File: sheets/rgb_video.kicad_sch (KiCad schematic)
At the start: 46 parts, among them CN3 DIN-8, U32 CXA1145P

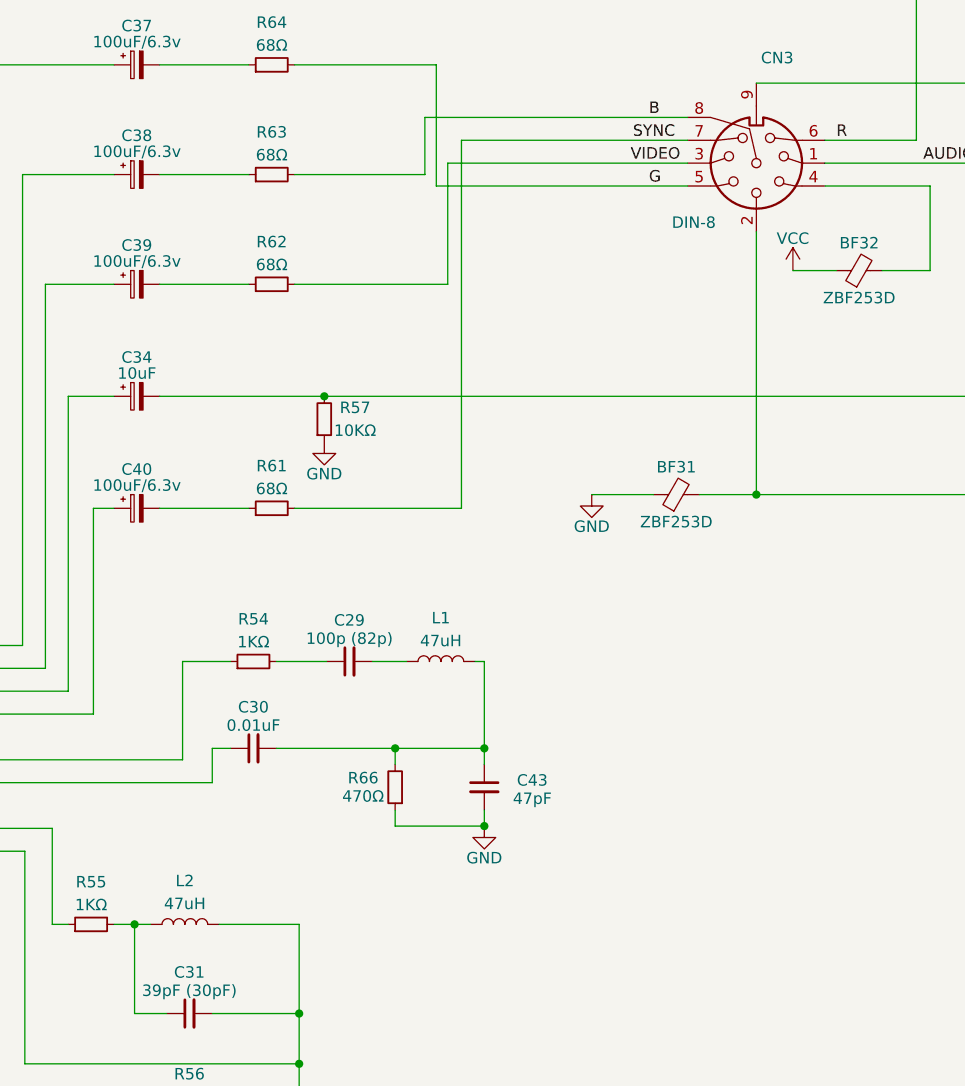
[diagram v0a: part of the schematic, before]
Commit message: Merged in schematics from stable with footprints
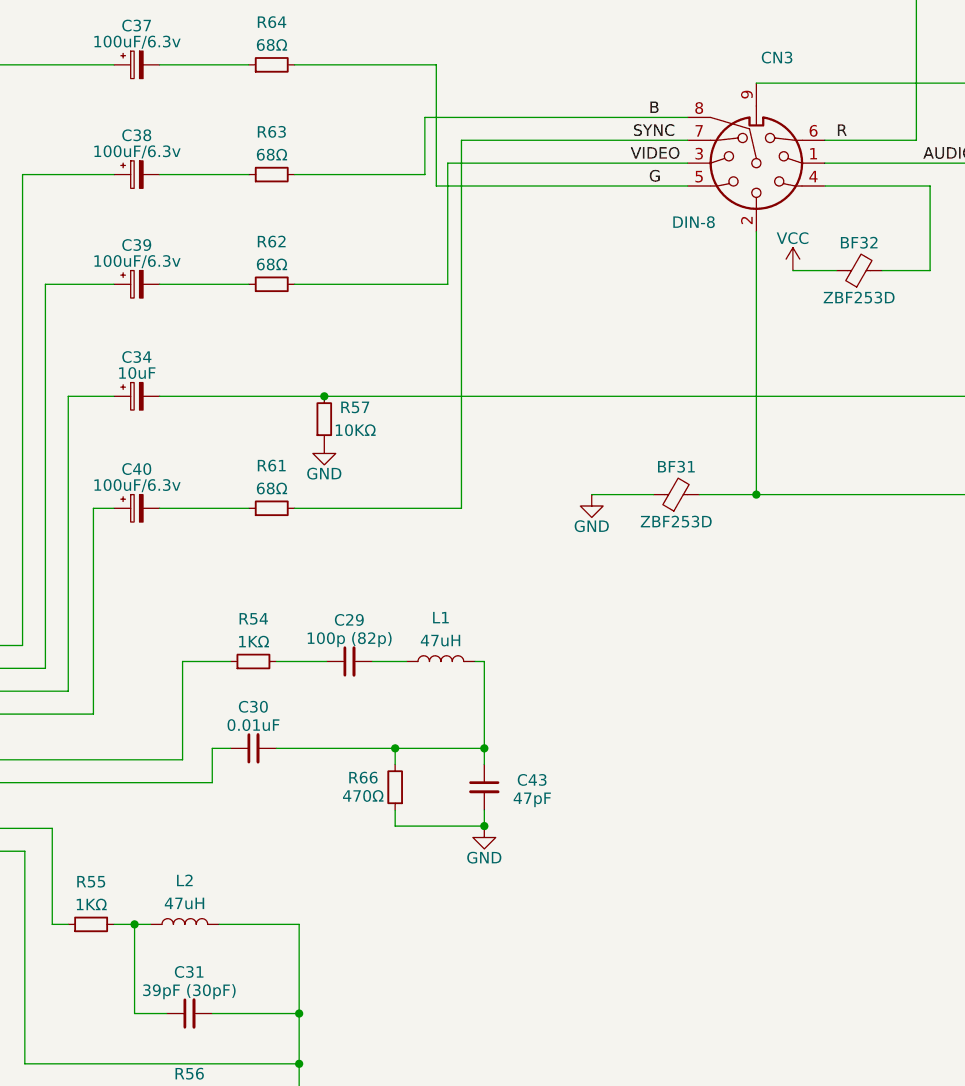
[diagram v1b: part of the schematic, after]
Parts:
- CN3: footprint (none) -> Connector_Dsub:DSUB-9_Female_Horizontal_P2.77x2.84mm_EdgePinOffset4.94mm_Housed_MountingHolesOffset7.48mm
- L1, L2: footprint (none) -> 1_NeoGeoLibrary:Resistor1-5mm
- U32: footprint (none) -> Package_DIP:DIP-24_W7.62mm

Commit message: Sync footprints from Nightly Build
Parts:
- C27, C28: footprint 1_NeoGeoLibrary:CAP1-5mm -> 1_NeoGeoLibrary:CAP3-5mm
- C35: footprint 1_NeoGeoLibrary:CAP3-5mm -> 1_NeoGeoLibrary:CAP2-2.5mm
- U32: footprint Package_DIP:DIP-24_W7.62mm -> Package_DIP:DIP-24_W10.16mm
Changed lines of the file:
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@@
     (property "Reference" "U32" (id 0) (at 200.914 144.272 0))
     (property "Value" "CXA1145P" (id 1) (at 213.106 193.802 0))
-    (property "Footprint" "Package_DIP:DIP-24_W7.62mm" (id 2) (at 213.106 169.418 0)
+    (property "Footprint" "Package_DIP:DIP-24_W10.16mm" (id 2) (at 213.106 169.418 0)
       (effects (font (size 1.27 1.27)) hide)
     )
@@
     (property "Reference" "C35" (id 0) (at 104.394 158.75 90))
     (property "Value" "4.7uf" (id 1) (at 104.394 160.528 90))
-    (property "Footprint" "1_NeoGeoLibrary:CAP3-5mm" (id 2) (at 104.394 163.068 0)
+    (property "Footprint" "1_NeoGeoLibrary:CAP2-2.5mm" (id 2) (at 104.394 163.068 0)
       (effects (font (size 1.27 1.27)) hide)
     )
@@
     (property "Reference" "C27" (id 0) (at 101.092 116.332 90))
     (property "Value" "0.1uF" (id 1) (at 101.092 118.364 90))
-    (property "Footprint" "1_NeoGeoLibrary:CAP1-5mm" (id 2) (at 101.092 121.412 0)
+    (property "Footprint" "1_NeoGeoLibrary:CAP3-5mm" (id 2) (at 101.092 121.412 0)
       (effects (font (size 1.27 1.27)) hide)
     )
@@
     (property "Reference" "C28" (id 0) (at 101.092 139.192 90))
     (property "Value" "0.1uF" (id 1) (at 101.092 141.224 90))
-    (property "Footprint" "1_NeoGeoLibrary:CAP1-5mm" (id 2) (at 101.092 144.272 0)
+    (property "Footprint" "1_NeoGeoLibrary:CAP3-5mm" (id 2) (at 101.092 144.272 0)
       (effects (font (size 1.27 1.27)) hide)
     )

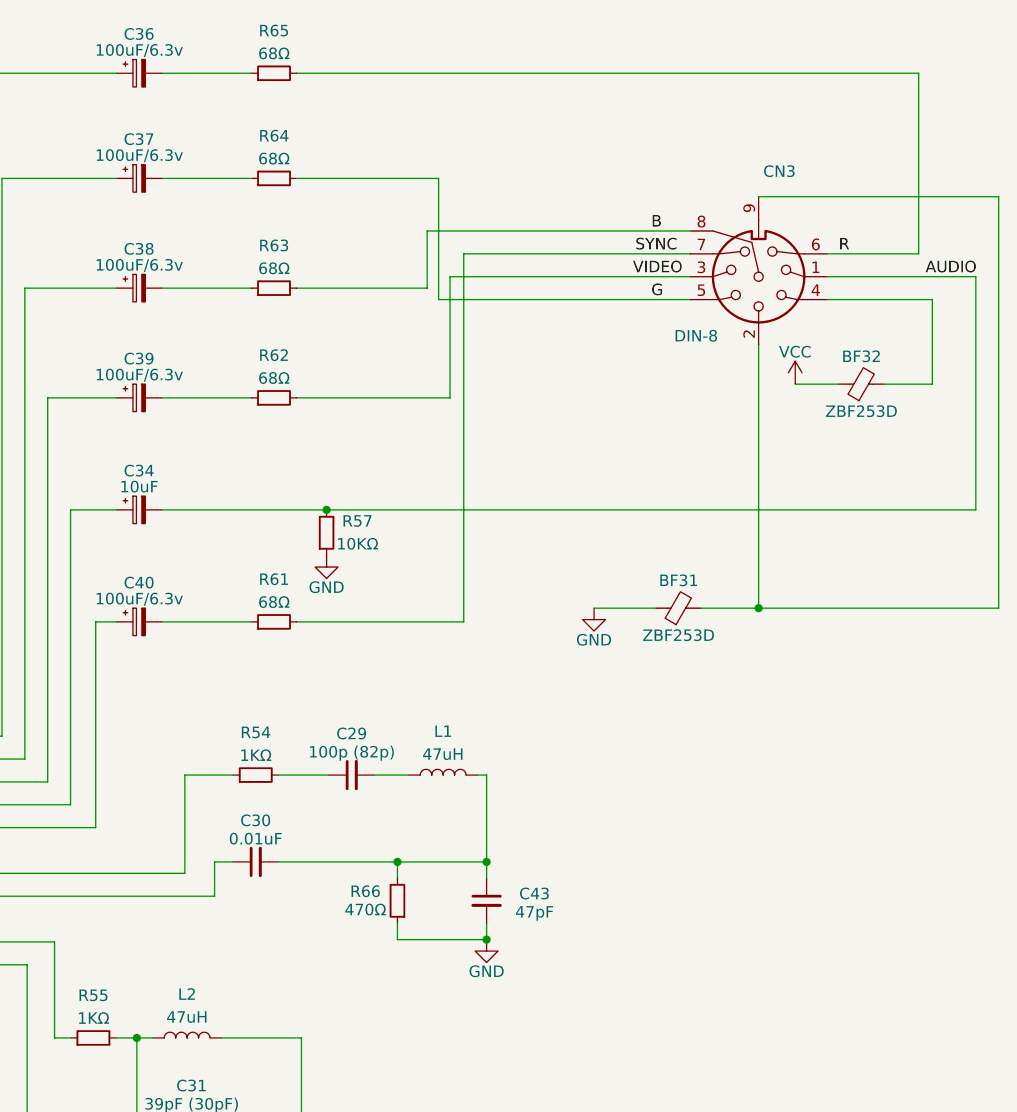
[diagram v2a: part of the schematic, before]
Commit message: 1. Swap Halt / Reset on RA1 2. Added more Power Caps 3. Change Audio socket Left/Right around 4. Added Ferrite Beads to Audio Signals 5. Added Ferrite Beads to Video Signals
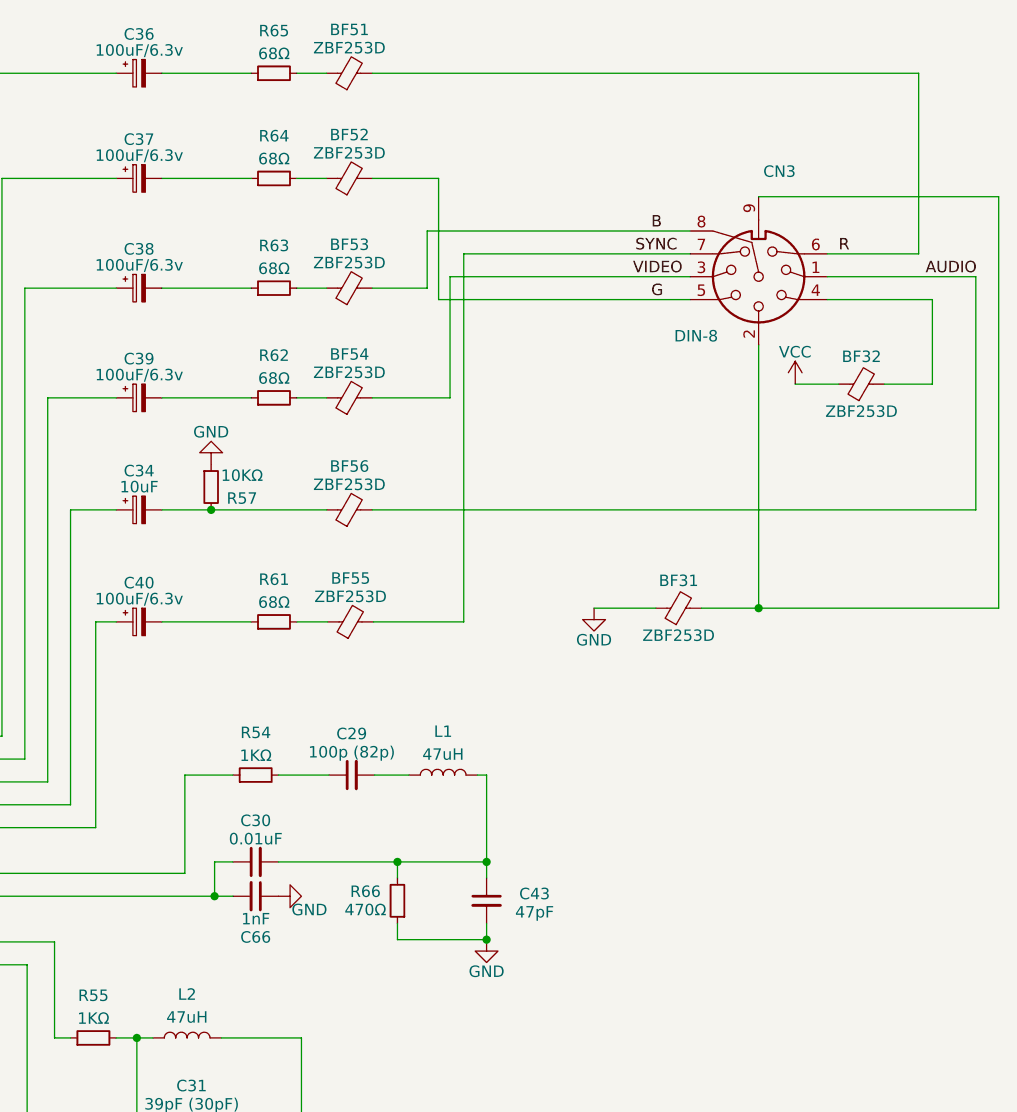
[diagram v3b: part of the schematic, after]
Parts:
- added BF51, BF52, BF53, BF54, BF55, BF56: ZBF253D, 1_NeoGeoLibrary:BF-2.5mm, symbol Device:FerriteBead_Small
- added C66: 1nF, 1_NeoGeoLibrary:CAP1-5mm, symbol Device:C_Small
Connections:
- net AUDIO: now also BF56.2; no longer C34.2, R57.2
- net B: now also BF53.2; no longer R63.2
- net G: now also BF52.2; no longer R64.2
- net GND: now also C66.1
- net R: now also BF51.2; no longer R65.2
- net SYNC: now also BF55.2; no longer R61.2
- net VIDEO: now also BF54.2; no longer R62.2
- net at C30.1, U32.17 (CIN): now also C66.2
- new net: BF54.1, R62.2
- new net: BF53.1, R63.2
- new net: BF52.1, R64.2
- new net: BF55.1, R61.2
- new net: BF56.1, C34.2, R57.2
- new net: BF51.1, R65.2
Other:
- moved on the sheet: R57

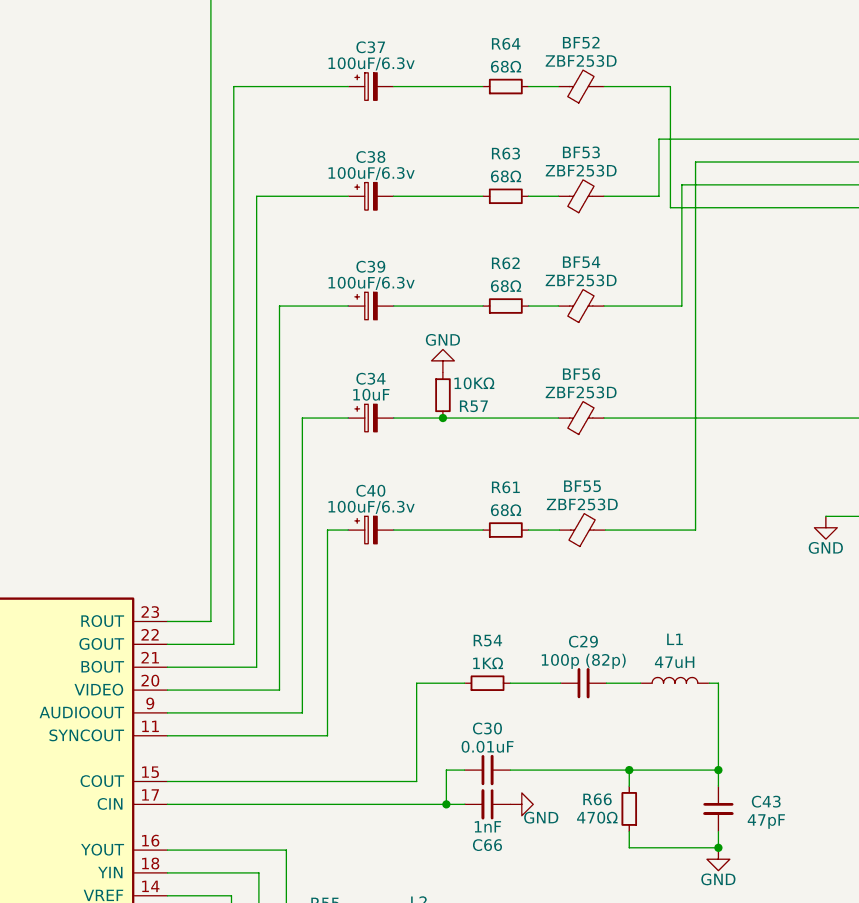
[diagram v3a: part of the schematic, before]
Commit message: Changed sync circuit not to use SYNCOUT pin 11 on CX Chip
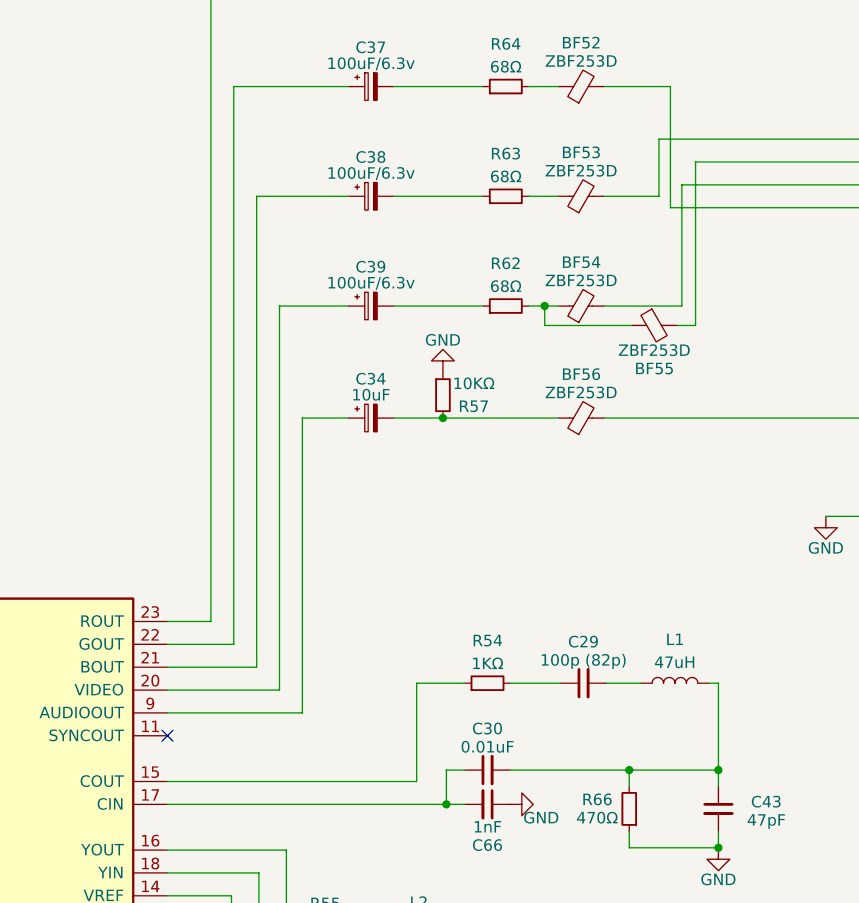
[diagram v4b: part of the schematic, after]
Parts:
- removed C40: 100uF/6.3v, 1_NeoGeoLibrary:CAP3-5mm, symbol Device:C_Polarized_Small
- removed R61: 68Ω, 1_NeoGeoLibrary:Resistor1-5mm, symbol Device:R_Small
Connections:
- net at BF54.1, R62.2: now also BF55.1
- no-connect marks 1 -> 2
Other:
- moved on the sheet: BF55
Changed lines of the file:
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@@
   (junction (at 292.1 164.338) (diameter 0) (color 0 0 0 0)
   )
+  (junction (at 272.796 112.776) (diameter 0) (color 0 0 0 0)
+  )
   (junction (at 237.998 205.232) (diameter 0) (color 0 0 0 0)
   )
@@
   )
   (no_connect (at 195.326 168.148))
+  (no_connect (at 230.886 160.528))
   (wire (pts (xy 341.63 111.252) (xy 336.296 111.252))
     (stroke (width 0) (type default) (color 0 0 0 0))
@@
     (stroke (width 0) (type default) (color 0 0 0 0))
   )
+  (wire (pts (xy 272.796 112.776) (xy 272.796 114.935))
+    (stroke (width 0) (type default) (color 0 0 0 0))
+  )
   (wire (pts (xy 245.872 125.222) (xy 250.952 125.222))
     (stroke (width 0) (type default) (color 0 0 0 0))
@@
     (stroke (width 0) (type default) (color 0 0 0 0))
   )
-  (wire (pts (xy 271.018 112.776) (xy 274.32 112.776))
+  (wire (pts (xy 271.018 112.776) (xy 272.796 112.776))
     (stroke (width 0) (type default) (color 0 0 0 0))
   )
@@
     (stroke (width 0) (type default) (color 0 0 0 0))
   )
-  (wire (pts (xy 248.666 160.528) (xy 248.666 137.668))
-    (stroke (width 0) (type default) (color 0 0 0 0))
-  )
   (wire (pts (xy 271.526 205.232) (xy 271.526 199.39))
     (stroke (width 0) (type default) (color 0 0 0 0))
@@
     (stroke (width 0) (type default) (color 0 0 0 0))
   )
-  (wire (pts (xy 289.56 137.668) (xy 289.56 96.774))
-    (stroke (width 0) (type default) (color 0 0 0 0))
-  )
-  (wire (pts (xy 271.018 137.668) (xy 274.447 137.668))
-    (stroke (width 0) (type default) (color 0 0 0 0))
-  )
   (wire (pts (xy 181.61 183.388) (xy 181.61 188.214))
     (stroke (width 0) (type default) (color 0 0 0 0))
@@
     (stroke (width 0) (type default) (color 0 0 0 0))
   )
+  (wire (pts (xy 287.528 114.935) (xy 289.56 114.935))
+    (stroke (width 0) (type default) (color 0 0 0 0))
+  )
   (wire (pts (xy 261.493 125.222) (xy 274.32 125.222))
     (stroke (width 0) (type default) (color 0 0 0 0))
@@
     (stroke (width 0) (type default) (color 0 0 0 0))
   )
+  (wire (pts (xy 272.796 114.935) (xy 282.448 114.935))
+    (stroke (width 0) (type default) (color 0 0 0 0))
+  )
   (wire (pts (xy 95.25 124.714) (xy 95.25 121.412))
     (stroke (width 0) (type default) (color 0 0 0 0))
   )
-  (wire (pts (xy 279.527 137.668) (xy 289.56 137.668))
-    (stroke (width 0) (type default) (color 0 0 0 0))
-  )
   (wire (pts (xy 144.018 170.688) (xy 152.4 170.688))
     (stroke (width 0) (type default) (color 0 0 0 0))
@@
     (stroke (width 0) (type default) (color 0 0 0 0))
   )
+  (wire (pts (xy 289.56 114.935) (xy 289.56 96.774))
+    (stroke (width 0) (type default) (color 0 0 0 0))
+  )
   (wire (pts (xy 244.094 183.896) (xy 244.094 173.228))
     (stroke (width 0) (type default) (color 0 0 0 0))
@@
     (stroke (width 0) (type default) (color 0 0 0 0))
   )
+  (wire (pts (xy 272.796 112.776) (xy 274.32 112.776))
+    (stroke (width 0) (type default) (color 0 0 0 0))
+  )
   (wire (pts (xy 240.792 152.908) (xy 240.792 100.584))
     (stroke (width 0) (type default) (color 0 0 0 0))
@@
     (stroke (width 0) (type default) (color 0 0 0 0))
   )
-  (wire (pts (xy 256.032 137.668) (xy 265.938 137.668))
-    (stroke (width 0) (type default) (color 0 0 0 0))
-  )
   (wire (pts (xy 258.572 154.686) (xy 258.572 165.608))
     (stroke (width 0) (type default) (color 0 0 0 0))
@@
     (stroke (width 0) (type default) (color 0 0 0 0))
   )
-  (wire (pts (xy 230.886 160.528) (xy 248.666 160.528))
-    (stroke (width 0) (type default) (color 0 0 0 0))
-  )
   (wire (pts (xy 304.038 136.144) (xy 310.896 136.144))
     (stroke (width 0) (type default) (color 0 0 0 0))
@@
   )
   (wire (pts (xy 288.036 112.776) (xy 288.036 99.314))
-    (stroke (width 0) (type default) (color 0 0 0 0))
-  )
-  (wire (pts (xy 248.666 137.668) (xy 250.952 137.668))
     (stroke (width 0) (type default) (color 0 0 0 0))
   )
@@
     (pin "2")
   )
-  (symbol (lib_id "Device:R_Small") (at 268.478 137.668 90) (unit 1)
-    (in_bom yes) (on_board yes)
-    (property "Reference" "R61" (id 0) (at 268.478 132.969 90))
-    (property "Value" "68Ω" (id 1) (at 268.478 135.509 90))
-    (property "Footprint" "1_NeoGeoLibrary:Resistor1-5mm" (id 2) (at 268.478 137.668 0)
-      (effects (font (size 1.27 1.27)) hide)
-    )
-    (property "Datasheet" "" (id 3) (at 268.478 137.668 0)
-      (effects (font (size 1.27 1.27)) hide)
-    )
-    (pin "1")
-    (pin "2")
-  )
   (symbol (lib_id "Device:C_Small") (at 101.092 121.412 90) (unit 1)
     (in_bom yes) (on_board yes)
@@
     (pin "2")
   )
-  (symbol (lib_id "Device:FerriteBead_Small") (at 276.987 137.668 90) (unit 1)
-    (in_bom yes) (on_board yes)
-    (property "Reference" "BF55" (id 0) (at 276.987 132.842 90))
-    (property "Value" "ZBF253D" (id 1) (at 276.987 134.874 90))
-    (property "Footprint" "1_NeoGeoLibrary:BF-2.5mm" (id 2) (at 276.987 139.446 90)
-      (effects (font (size 1.27 1.27)) hide)
-    )
-    (property "Datasheet" "" (id 3) (at 276.987 137.668 0)
+  (symbol (lib_id "Device:FerriteBead_Small") (at 284.988 114.935 90) (mirror x) (unit 1)
+    (in_bom yes) (on_board yes)
+    (property "Reference" "BF55" (id 0) (at 284.988 119.761 90))
+    (property "Value" "ZBF253D" (id 1) (at 284.988 117.729 90))
+    (property "Footprint" "1_NeoGeoLibrary:BF-2.5mm" (id 2) (at 284.988 113.157 90)
+      (effects (font (size 1.27 1.27)) hide)
+    )
+    (property "Datasheet" "" (id 3) (at 284.988 114.935 0)
       (effects (font (size 1.27 1.27)) hide)
     )
@@
     (pin "1")
   )
-  (symbol (lib_id "Device:C_Polarized_Small") (at 253.492 137.668 90) (mirror x) (unit 1)
-    (in_bom yes) (on_board yes)
-    (property "Reference" "C40" (id 0) (at 253.492 133.35 90))
-    (property "Value" "100uF/6.3v" (id 1) (at 253.492 135.128 90))
-    (property "Footprint" "1_NeoGeoLibrary:CAP3-5mm" (id 2) (at 253.492 137.668 0)
-      (effects (font (size 1.27 1.27)) hide)
-    )
-    (property "Datasheet" "" (id 3) (at 253.492 137.668 0)
-      (effects (font (size 1.27 1.27)) hide)
-    )
-    (pin "1")
-    (pin "2")
-  )
   (symbol (lib_id "Device:C_Polarized_Small") (at 253.492 100.584 90) (mirror x) (unit 1)
